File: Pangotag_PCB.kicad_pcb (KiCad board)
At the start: 6 copper layers, 23 x 18 mm, 90 parts, among them CN2 POGOPIN_2X04_P2.54_M, IC1 TLV3691IDPFR, IC2 TLV3691IDPFR, J1 USB_C_Receptacle, J2 Conn_Coaxial, J3 USB_B_Mini, J4 USB_A, J5 Conn_01x02, P1 USB_C_Plug, Q1 PMX100UNZ, Q2 PMX100UNZ, Q3 PMX100UNZ, Q4 PMX100UNZ, SW1 SW_Push, U1 TPS62840YBGR, U11 AS6221T-AWLT, U13 TPS62840YBGR, U14 BMP581, U15 TMUX1575YCJR, U16 BMI270, U18 TPS62840YBGR, U3 SN74AUP1G08DPWR, U4 STM32U585OIYxQ, U5 TMUX1575YCJR, U6 MIA-M10Q, U7 LTC2941IDCB-1#TRMPBF, Y1 CM9V-T1A-32.768KHZ-7PF-20PPM-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

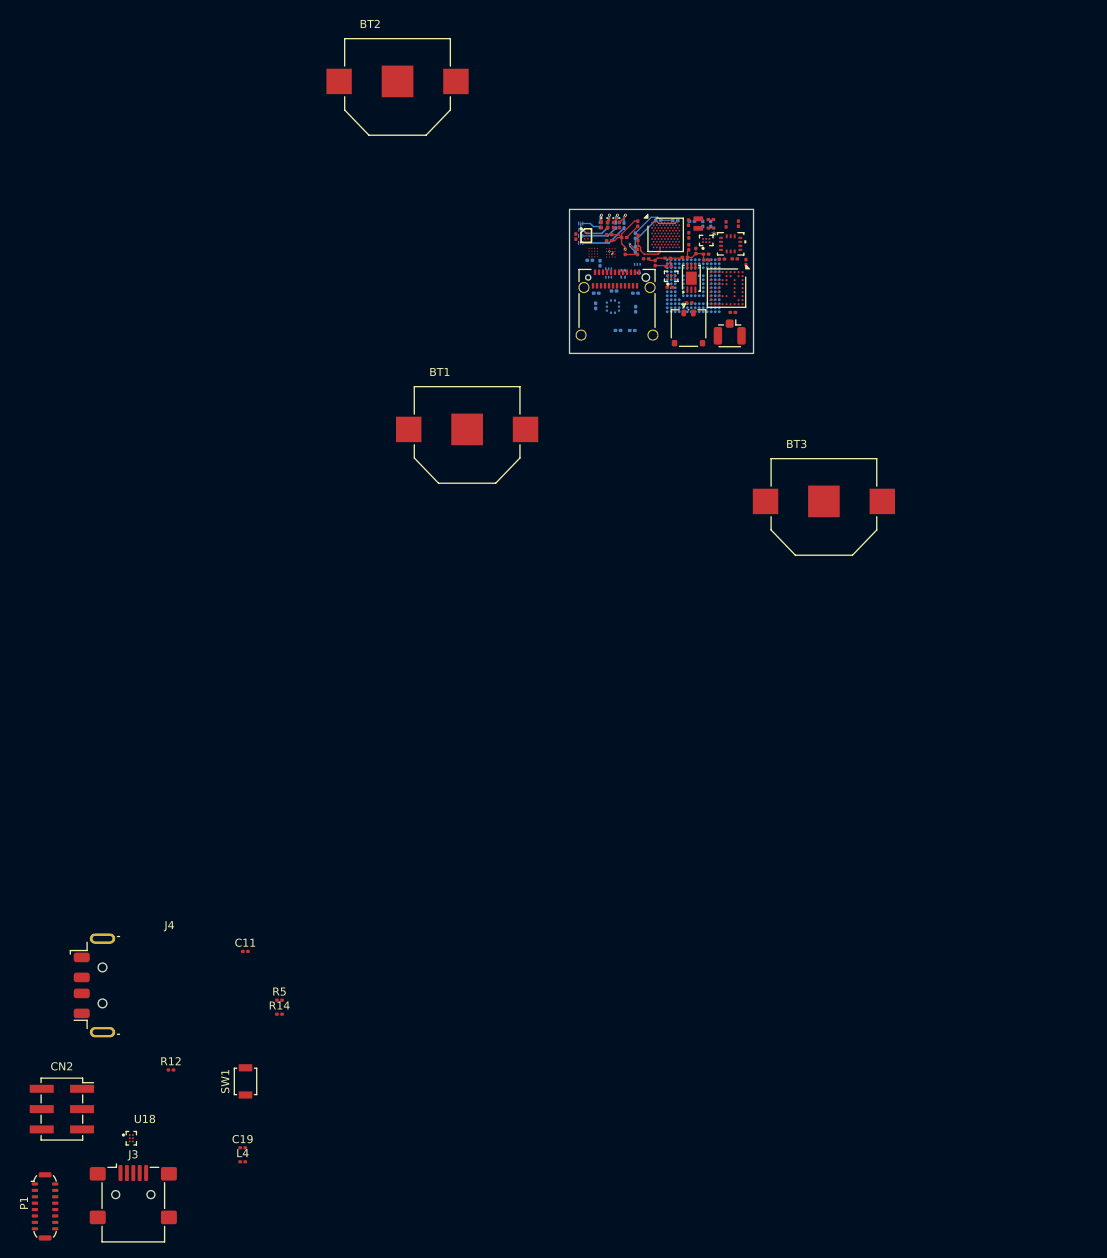
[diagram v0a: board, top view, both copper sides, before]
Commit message: Add V2: STM32U575 LQFP-64 tag board and ST-Link dongle
The tag moves from the 23 × 18 mm STM32U585 WLCSP-90 layout to a
31.94 × 27.18 mm, 6-layer board (Pangotag_PCB_LCSC_compat4.kicad_pcb) with
an LQFP-64 STM32U575, a MAX-M10S GNSS module, a 32 GB eMMC and parts that
JLCPCB stocks. Adds the USB-C debug dongle, the intermediate revisions, the
JLCPCB production files, the project footprint and symbol libraries, BOMs
and renders, plus a README.

Stops tracking KiCad lock files, the local-history folder and .DS_Store,
and ignores them along with large 3D exports.
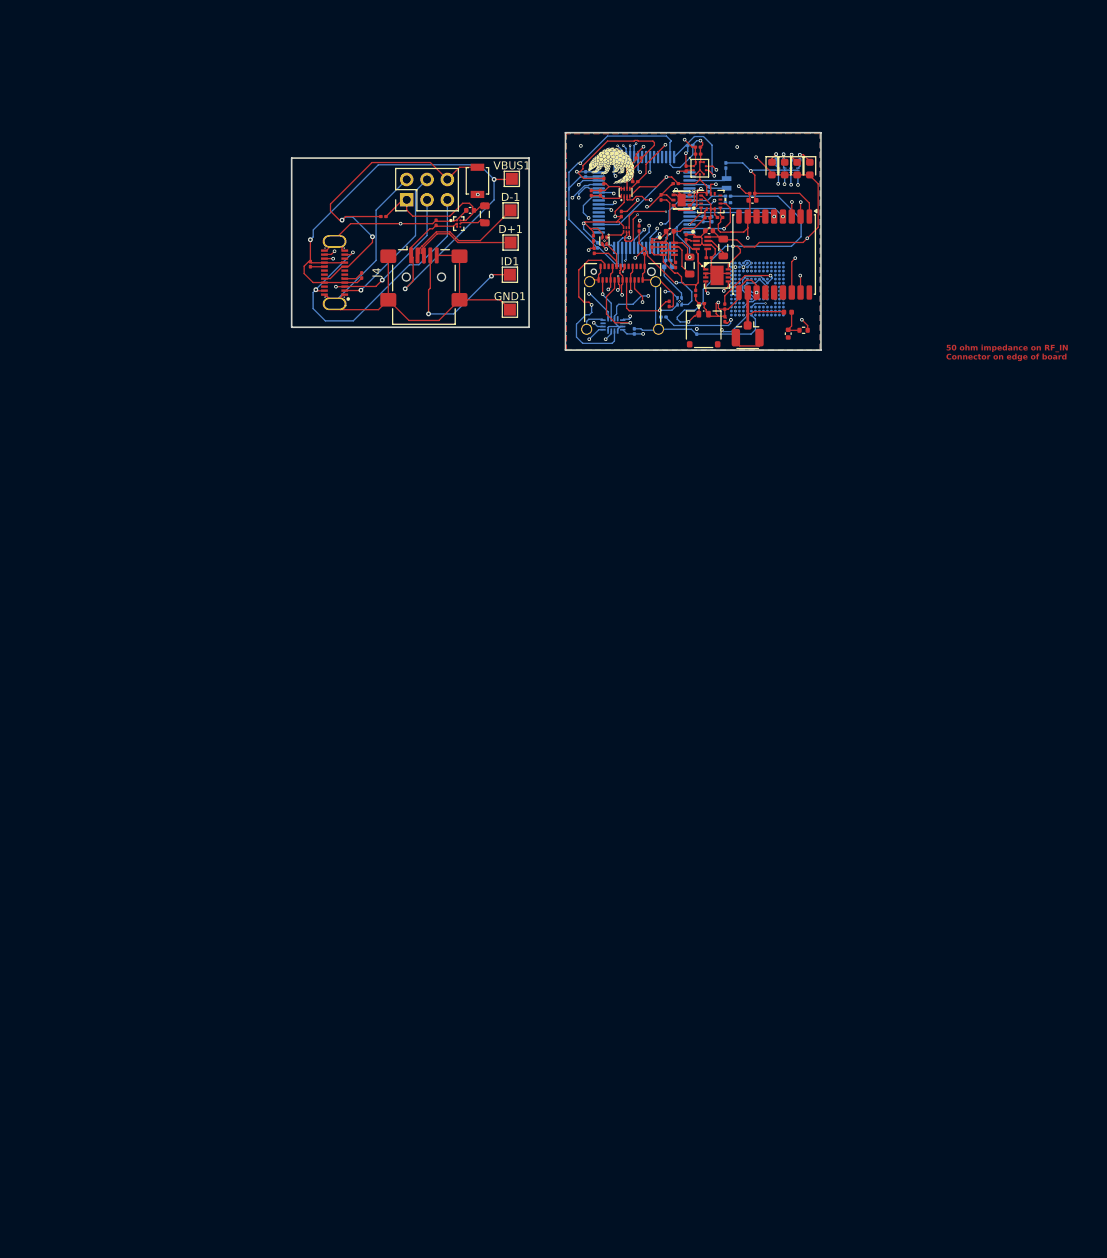
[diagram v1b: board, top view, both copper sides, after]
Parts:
- removed BT1, BT2, BT3: 2996, 2996:BAT_2996
- removed C12: 10u, Capacitor_SMD:C_0201_0603Metric
- removed C32: 2.2u, Capacitor_SMD:C_0201_0603Metric
- removed C34, C9: 4.7u, Capacitor_SMD:C_0201_0603Metric
- removed IC1, IC2: TLV3691IDPFR, TLV3691:TLV3691IDPFR
- removed L2, L3: 2.2u, Inductor_SMD:L_0201_0603Metric
- removed P1: USB_C_Plug, Connector_USB:USB_C_Plug_ShenzhenJingTuoJin_918-118A2021Y40002_Vertical
- removed U11: AS6221T-AWLT, AS6221T:BGA6C40P2X3_102X150X52
- removed U13: TPS62840YBGR, TPS62840YBGR:BGA6N40P3X2_146X96X50N
- removed U15: TMUX1575YCJR, TMUX1575YCJR:PREYCJ0016-IPC_A
- added C39: 100n, Capacitor_SMD:C_0201_0603Metric, B.Cu at (90.5, 48.5)
- added C4: 10n, Capacitor_SMD:C_0402_1005Metric, F.Cu at (114.3, 59.5)
- added C40: 100n, Capacitor_SMD:C_0201_0603Metric, B.Cu at (99.3, 50.4)
- added C8: 4.7u, Capacitor_SMD:C_0201_0603Metric, F.Cu at (97.3, 48.4)
- added D+1: MountingHole_Pad, TestPoint:TestPoint_Pad_1.5x1.5mm, F.Cu at (79.6, 48.1)
- added D-1: MountingHole_Pad, TestPoint:TestPoint_Pad_1.5x1.5mm, F.Cu at (79.6, 44.1)
- added GND1: MountingHole_Pad, TestPoint:TestPoint_Pad_1.5x1.5mm, F.Cu at (79.5, 56.5)
- added IC3: TPS62840DLCR, TPS62840DLCR:SON50P150X200X100-8N-D, F.Cu at (103.6, 48.2)
- added IC4: TPS62840DLCR, TPS62840DLCR:SON50P150X200X100-8N-D, F.Cu at (99.4, 48.9)
- added ID1: MountingHole_Pad, TestPoint:TestPoint_Pad_1.5x1.5mm, F.Cu at (79.5, 52.2)
- added L7: 2.2u, Inductor_SMD:L_0805_2012Metric, F.Cu at (102.0, 51.0)
- added R10: 56k, Resistor_SMD:R_0201_0603Metric, F.Cu at (61.0, 52.3)
- added R17: 56k, Resistor_SMD:R_0201_0603Metric, F.Cu at (54.6, 50.8)
- added R18: 200k, Resistor_SMD:R_0201_0603Metric, F.Cu at (91.3, 40.5)
- added R19: 10k, Resistor_SMD:R_0201_0603Metric, F.Cu at (95.7, 37.6)
- added R20: 10k, Resistor_SMD:R_0201_0603Metric, F.Cu at (95.2, 40.5)
- added R23: 50m, Resistor_SMD:R_0201_0603Metric, F.Cu at (102.8, 54.4)
- added U10: TLV7031DPWR, easyeda2kicad:X2SON-4_L0.8-W0.8-P0.48-TL-A, B.Cu at (100.8, 55.5)
- added U8: PCA9306DQER, easyeda2kicad:X2SON-8_L1.4-W1.0-P0.35-BL, F.Cu at (94.0, 41.9)
- added U9: TLV7031DPWR, easyeda2kicad:X2SON-4_L0.8-W0.8-P0.48-TL-A, F.Cu at (91.4, 47.9)
- added VBUS1: MountingHole_Pad, TestPoint:TestPoint_Pad_1.5x1.5mm, F.Cu at (79.8, 40.2)
- C1, C10, C15, C2, R21, R22, R3, R4, U14: moved to F.Cu
- C14: value 10u -> 100n
- C16, C17, C28, C29, C36, Y1: moved to B.Cu
- C19, C22, C25: footprint Capacitor_SMD:C_0201_0603Metric -> Capacitor_SMD:C_0402_1005Metric
- C24, C35: value 100n -> 10u; footprint Capacitor_SMD:C_0201_0603Metric -> Capacitor_SMD:C_0402_1005Metric
- C30: value 10u -> 100p
- C31: value 2.2u -> 100n; moved to B.Cu
- C33: value 100n -> 4.7u
- C37: value 1u -> 100n
- CN2: footprint Connector_PinSocket_2.54mm:PinSocket_2x03_P2.54mm_Vertical_SMD -> Connector_PinHeader_2.54mm:PinHeader_2x03_P2.54mm_Vertical
- D1, D2, D3, D4: footprint LED_SMD:LED_0201_0603Metric -> LED_SMD:LED_0603_1608Metric
- J4: value USB_A -> UP32-C-F-G-FL-3-P24-TR; footprint Connector_USB:USB_A_Molex_48037-2200_Horizontal -> easyeda2kicad:USB-TH-TYPE-C_00702-UCAM002-X
- L1: value 100n -> 27n; footprint Inductor_SMD:L_0201_0603Metric -> Inductor_SMD:L_0402_1005Metric
- L4, L5: footprint Inductor_SMD:L_0201_0603Metric -> Inductor_SMD:L_0805_2012Metric
- R14: value 56k -> 909
- R5: value 56k -> 10; footprint Resistor_SMD:R_0201_0603Metric -> Resistor_SMD:R_0402_1005Metric
- U1: value TPS62840YBGR -> 74AUP1G08GS_132; footprint TPS62840YBGR:BGA6N40P3X2_146X96X50N -> 74AUP1G08GS:XSON6_SOT1202_NEX
- U3: value SN74AUP1G08DPWR -> T117_C19284874; footprint SN74AUP1G08:DPW0005A_TEX -> easyeda2kicad:TDFN-6_L2.0-W2.0-P0.65-TL-EP; moved to F.Cu
- U4: value STM32U585OIYxQ -> MAX-M10S; footprint Package_CSP:ST_WLCSP-90_4.2x3.95mm_Layout18x10_P0.4mm_Stagger -> RF_GPS:ublox_MAX
- U5: value TMUX1575YCJR -> STM32U575RGTx; footprint TMUX1575YCJR:PREYCJ0016-IPC_A -> Package_QFP:LQFP-64_10x10mm_P0.5mm; moved to B.Cu
- U6: value MIA-M10Q -> LTC2944IDD#PBF; footprint Package_LGA:ublox_LGA-53_4.5x4.5mm_Layout9x9_P0.5mm -> easyeda2kicad:DFN-8_L3.0-W3.0-P0.50-BL-EP
- U7: value LTC2941IDCB-1#TRMPBF -> TMUX1511RSVR; footprint Package_DFN_QFN:DFN-6-1EP_3x2mm_P0.5mm_EP1.65x1.35mm -> easyeda2kicad:UTQFN-16_L2.6-W1.8-P0.40-BL; moved to B.Cu
- moved L4 122.2 mm to (76.4, 44.6), turned to 90 degrees
- moved CN2 121.6 mm to (66.7, 42.8), turned to 90 degrees
- moved U18 121.4 mm to (73.2, 45.8)
- moved C19 120.6 mm to (74.6, 44.1), turned to 180 degrees
- moved J3 120.3 mm to (68.8, 52.5)
- moved SW1 116.2 mm to (75.5, 40.4), turned to -90 degrees
- moved R12 109.9 mm to (63.7, 44.9), turned to 180 degrees
- moved R5 106.3 mm to (116.3, 59.1), turned to 180 degrees
- moved R14 105.9 mm to (100.3, 51.0), turned to -90 degrees
- moved C11 94.1 mm to (70.3, 45.7), turned to 90 degrees
- moved J4 91.5 mm to (57.6, 51.9), turned to -90 degrees
- moved Q4 28.6 mm to (115.5, 39.1), turned to 90 degrees
- moved Q3 27.5 mm to (114.7, 39.1), turned to 90 degrees
- moved Q2 26.6 mm to (113.9, 39.1), turned to 90 degrees
- moved Q1 25.6 mm to (113.1, 39.1), turned to 90 degrees
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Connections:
- C11 pad 2: GND -> GND2
- C14 pad 1: VDDA -> Net-(U8-EN)
- C19 pad 2: GND -> GND2
- C24 pad 1: GND -> +3V3
- C24 pad 2: VDDA -> GND
- C25 pad 1: GND -> VDDA
- C25 pad 2: VDDA -> GND
- C26 pad 1: GND -> VDDA
- C26 pad 2: VDDA -> GND
- C27 pad 1: GND -> VDDA
- C27 pad 2: VDDA -> GND
- C28 pad 1: GND -> VDDA
- C28 pad 2: VDDA -> GND
- C30 pad 1: GND -> Net-(U8-EN)
- C30 pad 2: VDDA -> GND
- C31 pad 1: Net-(C31-Pad1) -> VDDA
- C33 pad 1: GND -> Net-(U5-VCAP)
- C33 pad 2: VDDA -> GND
- CN2 pad 2: GND -> GND2
- J1 pad A11: Net-(J1-RX2+) -> unconnected-(J1-RX2+-PadA11)
- J1 pad A3: Net-(J1-TX1-) -> unconnected-(J1-TX1--PadA3)
- J1 pad A6: USB_OTG_FS_DP -> USB_OTG_FS_D+
- J1 pad A7: USB_OTG_FS_DM -> USB_OTG_FS_D-
- J1 pad A8: Net-(J1-SBU1) -> unconnected-(J1-SBU1-PadA8)
- J1 pad B2: Net-(J1-TX2+) -> unconnected-(J1-TX2+-PadB2)
- J1 pad B6: USB_OTG_FS_DP -> USB_OTG_FS_D+
- J1 pad B7: USB_OTG_FS_DM -> USB_OTG_FS_D-
- J3 pad 2: Net-(J3-D-) -> ST_D-
- J3 pad 3: Net-(J3-D+) -> ST_D+
- J3 pad 4: unconnected-(J3-ID-Pad4) -> Net-(J3-ID)
- J3 pad 5: GND -> GND2
- J3 pad SH: GND -> GND2
- L1 pad 1: +3V3 -> Net-(C4-Pad1)
- L5 pad 1: VLXSMPS -> +3V3
- L5 pad 2: Net-(C31-Pad1) -> Net-(IC3-SW)
- R12 pad 1: VDDA -> +1V8_2
- R12 pad 2: NRST -> NRST_OUT
- R13 pad 1: Net-(U1-VSET) -> Net-(IC3-VSET)
- R14 pad 1: VBUS_DONGLE -> Net-(IC4-VSET)
- R14 pad 2: Net-(P1-VCONN) -> GND
- R5 pad 1: VBUS_DONGLE -> +3V3
- R5 pad 2: Net-(P1-CC) -> Net-(C4-Pad1)
- SW1 pad 1: NRST -> NRST_OUT
- SW1 pad 2: GND -> GND2
- U18 pad A1: GND -> GND2
- U18 pad C2: GND -> GND2
- U3 pad 1: Net-(IC1-OUT) -> I2C1_SCL
- U3 pad 2: Net-(IC2-OUT) -> GND
- U3 pad 3: GND -> unconnected-(U3-ALERT-Pad3)
- U3 pad 4: USBC_FUNCTION -> GND
- U5 pad 1: SWCLK -> unconnected-(U5-VBAT-Pad1)
- U5 pad 10: USBC_FUNCTION -> Timepulse
- U5 pad 11: GND -> GPS_EXTINT
- U5 pad 12: unconnected-(U5-S4B-Pad12) -> GND
- U5 pad 13: Net-(J1-TX1+) -> VDDA
- U5 pad 14: Net-(J1-TX2+) -> ACC_INT1
- U5 pad 15: Net-(J1-SBU1) -> ACC_INT2
- U5 pad 16: Net-(J1-SBU2) -> unconnected-(U5-PA2-Pad16)
- U5 pad 2: SWCLK -> unconnected-(U5-PC13-Pad2)
- U5 pad 3: unconnected-(U5-S1B-Pad3) -> OSC32_IN
- U5 pad 4: unconnected-(U5-S2B-Pad4) -> OSC32_OUT
- U5 pad 5: NRST -> unconnected-(U5-PH0-Pad5)
- U5 pad 6: VDDA -> unconnected-(U5-PH1-Pad6)
- U5 pad 7: VDDA -> NRST
- U5 pad 8: unconnected-(U5-S3B-Pad8) -> VBAT/3
- U5 pad 9: NRST -> PRS_INT
- U7 pad 1: VDD -> USBC_FUNCTION
- U7 pad 2: GND -> Net-(J1-TX1+)
- U7 pad 3: I2C1_SCL -> SWCLK
- U7 pad 4: I2C1_SDA -> USBC_FUNCTION
- U7 pad 5: unconnected-(U7-AL#/CC-Pad5) -> Net-(J1-TX2-)
- U7 pad 6: VDD2 -> SWDIO
- U7 pad 7: GND -> unconnected-(U7-N.C.-Pad7)
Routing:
- net GND: track 19.9 -> 274.8 mm, vias 0 -> 15
- net VDDA: track 19.7 -> 166.4 mm, vias 2 -> 14
- net +3V3: track 2.59 -> 112.2 mm, vias 1 -> 5
- net GND2: track 0.00 -> 84.2 mm, vias 0 -> 2
- net VBUS_DONGLE: track 0.00 -> 78.4 mm, vias 0 -> 3
- net I2C1_SCL: track 0.00 -> 69.0 mm, vias 0 -> 6
- net I2C1_SDA: track 0.00 -> 63.9 mm, vias 0 -> 2
- net VDD: track 0.00 -> 44.6 mm, vias 0 -> 2
- net NRST_OUT: track 0.00 -> 43.7 mm, vias 0 -> 2
- net SDMMC1_D1: track 0.00 -> 41.4 mm, vias 0 -> 2
- net SWO_OUT: track 0.00 -> 37.9 mm, vias 0 -> 2
- net SDMMC1_D0: track 0.00 -> 37.2 mm, vias 0 -> 2
- net SDMMC1_D2: track 0.00 -> 35.2 mm, vias 0 -> 2
- net I2C1_SDA_3V3: track 0.00 -> 33.4 mm, vias 0 -> 2
- net USB_OTG_FS_D+: track 0.00 -> 33.4 mm, vias 0 -> 2
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- added copper zone on B.Cu, net GND
- added copper zone on F.Cu, net GND
- added copper zone on In1.Cu, net GND2
- added copper zone on In3.Cu, net VDDA
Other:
- board size 23 x 18 mm -> 66.2 x 27.2 mm
- board text added: "50 ohm impedance on RF_IN Connector on edge of board"
